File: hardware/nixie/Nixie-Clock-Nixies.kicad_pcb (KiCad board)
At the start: 2 copper layers, 21 parts, among them J1 Nixies-Connector

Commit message: Add screw terminals for I/O, Improve PCB layout
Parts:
- moved J1 91.8 mm to (237.5, 64.8)
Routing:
- net /a2: track 94.3 -> 181.4 mm
- net /a1: track 97.5 -> 182.3 mm
- net /a3: track 19.4 -> 100.6 mm
- net /a4: track 18.3 -> 99.1 mm
- net /a5: track 74.9 -> 28.6 mm
- net /a6: track 74.4 -> 30.9 mm
- net /c6: track 270.5 -> 232.1 mm
- net /c1: track 228.9 -> 209.0 mm
- net /da: track 107.4 -> 126.0 mm
- net Net-(N6-PadA3): track 29.2 -> 44.3 mm
- net /c3: track 240.3 -> 227.5 mm
- net /c4: track 237.2 -> 225.9 mm
- net /c2: track 242.3 -> 232.6 mm
- net Net-(N4-PadA3): track 48.5 -> 39.4 mm
- net /c5: track 224.6 -> 218.3 mm
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
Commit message: Add Mounting Holes to PCB, Improve Routing, Add power pin header, Use correct connector footprint
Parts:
- added H1: MountingHole, MountingHole:MountingHole_2.7mm_M2.5, F.Cu at (25.4, 24.1)
- added H2: MountingHole, MountingHole:MountingHole_2.7mm_M2.5, F.Cu at (243.8, 24.1)
- added H3: MountingHole, MountingHole:MountingHole_2.7mm_M2.5, F.Cu at (25.4, 58.4)
- added H4: MountingHole, MountingHole:MountingHole_2.7mm_M2.5, F.Cu at (243.8, 58.4)
- J1: footprint Connector_PinHeader_2.54mm:PinHeader_2x10_P2.54mm_Horizontal -> nixie-clock:PinHeader_2x10_P2.54mm_Horizontal_with_Interlock
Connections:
- J1 pad 18: Net-(J1-Pad18) -> (no net)
- J1 pad 7: Net-(J1-Pad7) -> (no net)

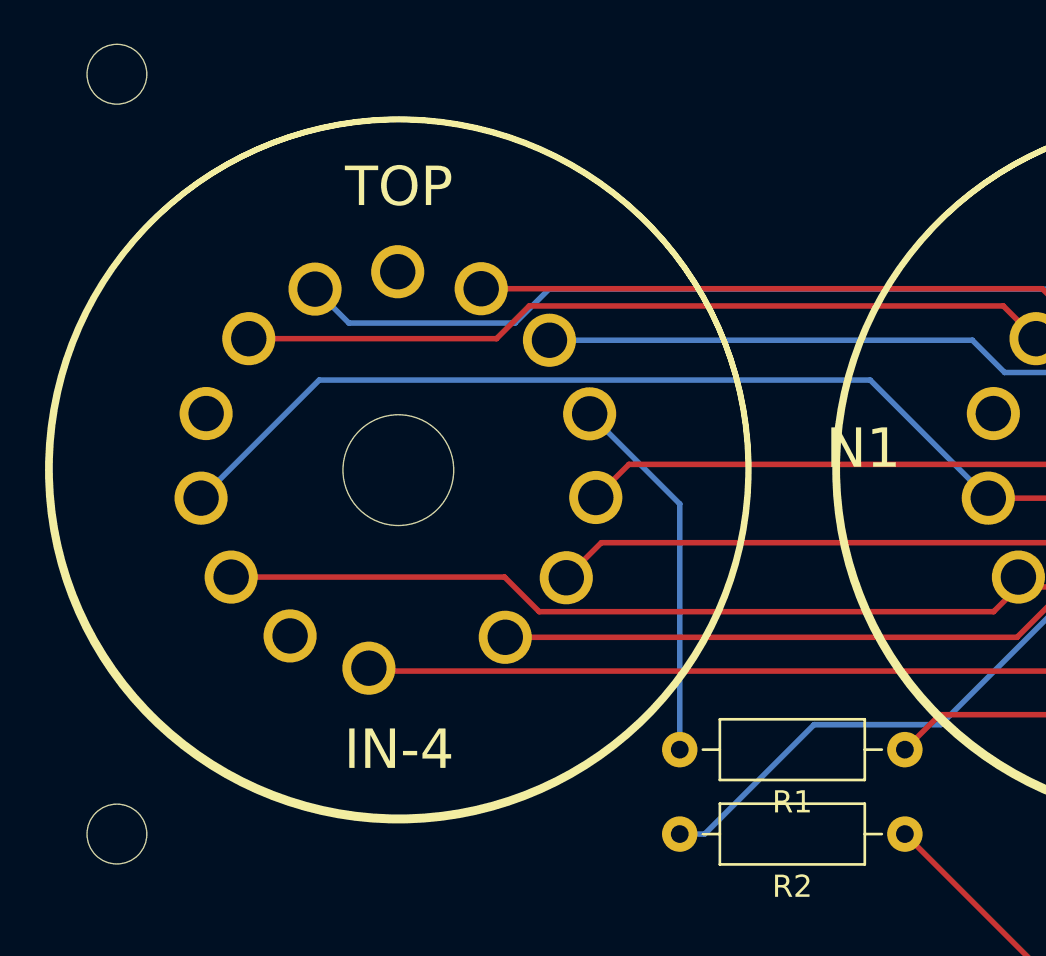
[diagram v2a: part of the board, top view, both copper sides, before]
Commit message: Fix libraries used in Nixie-Clock-Nixies
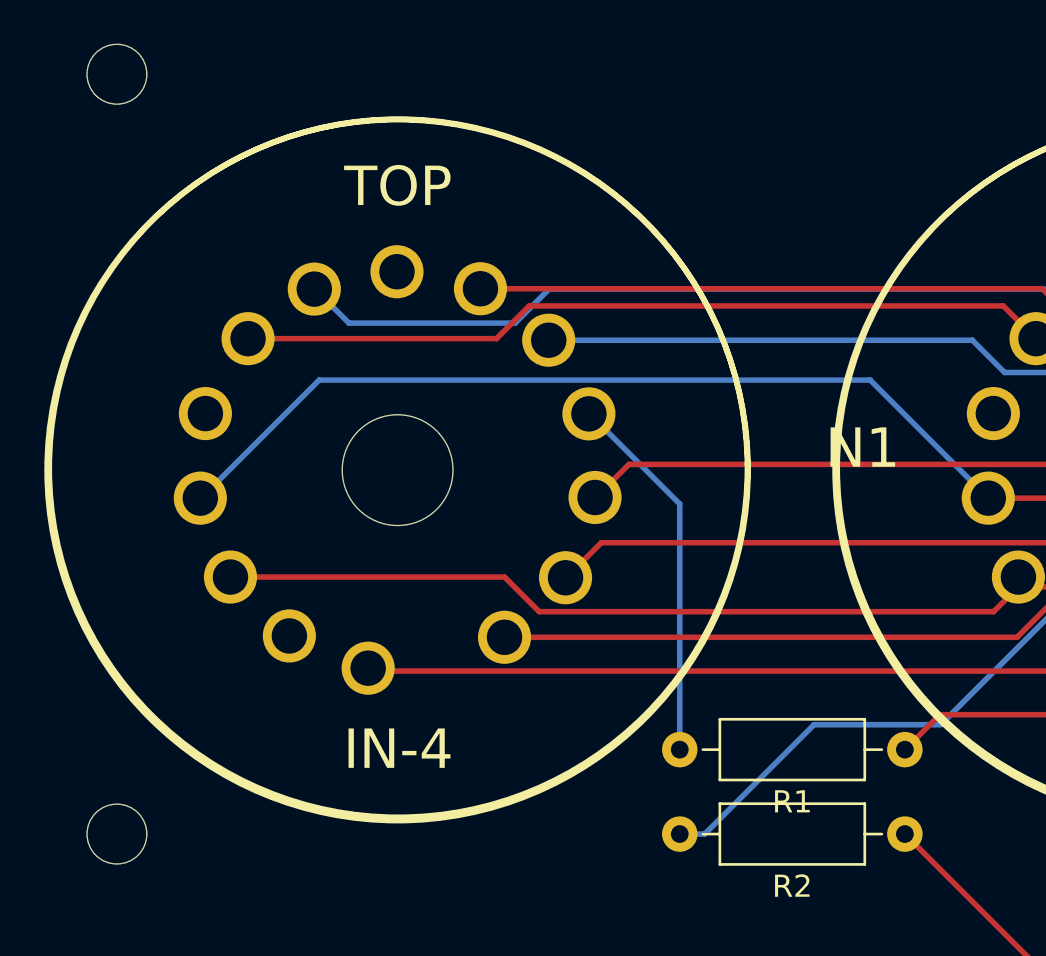
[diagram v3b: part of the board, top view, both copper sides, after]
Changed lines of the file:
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@@
   )
   (page A4)
+  (title_block
+    (title "Nixie-Clock: Nixies")
+    (date 2021-12-25)
+    (rev 1.0)
+    (company "Konrad Mösch")
+  )
   (layers
     (0 F.Cu signal)
@@
     (add_net /da)
     (add_net /dc)
-    (add_net "Net-(J1-Pad18)")
-    (add_net "Net-(J1-Pad7)")
     (add_net "Net-(N1-PadA3)")
     (add_net "Net-(N10-PadA)")
@@
     (add_net "Net-(N9-PadA)")
   )
+  (module nixies-us:nixies-us-IN-4-DSUB (layer F.Cu)
+    (at 38.1 41.91)
+    (descr "MAY BE USED WITH SOCKET: PL31-P")
+    (tags "MAY BE USED WITH SOCKET: PL31-P")
+    (attr virtual)
+    (fp_text reference N1 (at 20.955 -0.889) (layer F.SilkS)
+      (effects (font (size 1.778 1.778) (thickness 0.1524)))
+    )
+    (fp_text value IN-4 (at 0 12.7) (layer F.SilkS)
+      (effects (font (size 1.778 1.778) (thickness 0.1524)))
+    )
+    (fp_circle (center 0 0) (end 0 -2.54) (layer F.Mask) (width 0.0254))
+    (fp_circle (center 0 0) (end 0 -1.27) (layer F.Mask) (width 2.54))
+    (fp_circle (center 0 0) (end 0 -1.27) (layer B.Mask) (width 2.54))
+    (fp_circle (center -0.03302 0.08636) (end -0.03302 -2.45364) (layer Dwgs.User) (width 0.0254))
+    (fp_circle (center -0.03302 0.08636) (end -0.03302 -15.73022) (layer F.SilkS) (width 0.254))
+    (fp_circle (center 0 0) (end 0 -15.75308) (layer F.SilkS) (width 0.254))
+    (fp_text user TOP (at 0 -12.7) (layer F.SilkS)
+      (effects (font (size 1.778 1.778) (thickness 0.1524)))
+    )
+    (pad "" np_thru_hole circle (at -0.03302 0.08636) (size 4.99872 4.99872) (drill 4.99872) (layers *.Cu *.Mask))
+    (pad N/C thru_hole circle (at -0.06096 -8.86714) (size 2.39776 2.39776) (drill 1.59766) (layers *.Cu *.Mask))
+    (pad A3 thru_hole circle (at 8.60044 -2.45364) (size 2.39776 2.39776) (drill 1.59766) (layers *.Cu *.Mask)
+      (net 19 "Net-(N1-PadA3)"))
+    (pad A2 thru_hole circle (at -8.70712 -2.46634) (size 2.39776 2.39776) (drill 1.59766) (layers *.Cu *.Mask))
+    (pad A1 thru_hole circle (at -4.91744 7.5692) (size 2.39776 2.39776) (drill 1.59766) (layers *.Cu *.Mask))
+    (pad 9 thru_hole circle (at 6.78688 -5.77596) (size 2.39776 2.39776) (drill 1.59766) (layers *.Cu *.Mask)
+      (net 7 /c9))
+    (pad 8 thru_hole circle (at 8.8773 1.3208) (size 2.39776 2.39776) (drill 1.59766) (layers *.Cu *.Mask)
+      (net 8 /c8))
+    (pad 7 thru_hole circle (at 3.70586 -8.10006) (size 2.39776 2.39776) (drill 1.59766) (layers *.Cu *.Mask)
+      (net 9 /c7))
+    (pad 6 thru_hole circle (at 7.54634 4.94284) (size 2.39776 2.39776) (drill 1.59766) (layers *.Cu *.Mask)
+      (net 10 /c6))
+    (pad 5 thru_hole circle (at -7.57682 4.91236) (size 2.39776 2.39776) (drill 1.59766) (layers *.Cu *.Mask)
+      (net 11 /c5))
+    (pad 4 thru_hole circle (at 4.79298 7.63016) (size 2.39776 2.39776) (drill 1.59766) (layers *.Cu *.Mask)
+      (net 12 /c4))
+    (pad 3 thru_hole circle (at -8.93572 1.35128) (size 2.39776 2.39776) (drill 1.59766) (layers *.Cu *.Mask)
+      (net 13 /c3))
+    (pad 2 thru_hole circle (at -6.7818 -5.84708) (size 2.39776 2.39776) (drill 1.59766) (layers *.Cu *.Mask)
+      (net 14 /c2))
+    (pad 1 thru_hole circle (at -1.36144 9.02462) (size 2.39776 2.39776) (drill 1.59766) (layers *.Cu *.Mask)
+      (net 15 /c1))
+    (pad 0 thru_hole circle (at -3.79222 -8.08228) (size 2.39776 2.39776) (drill 1.59766) (layers *.Cu *.Mask)
+      (net 16 /c0))
+  )
   (module nixie-clock:PinHeader_2x10_P2.54mm_Horizontal_with_Interlock (layer F.Cu)
     (at 237.49 64.77 270)
@@
     )
     (fp_text value Nixies-Connector (at 5.655 25.13 90) (layer F.Fab)
-      (effects (font (size 1 1) (thickness 0.15)))
-    )
-    (fp_text user %R (at 5.31 11.43) (layer F.Fab)
       (effects (font (size 1 1) (thickness 0.15)))
     )
@@
     (fp_line (start -2.54 34.29) (end 15.24 34.29) (layer F.SilkS) (width 0.12))
     (fp_line (start 15.24 -11.43) (end 15.24 34.29) (layer F.SilkS) (width 0.12))
+    (fp_text user %R (at 5.31 11.43) (layer F.Fab)
+      (effects (font (size 1 1) (thickness 0.15)))
+    )
     (pad 20 thru_hole oval (at 2.54 22.86 270) (size 1.7 1.7) (drill 1) (layers *.Cu *.Mask)
       (net 17 /dc))
@@
       (effects (font (size 1 1) (thickness 0.15)))
     )
-    (fp_text user %R (at 0.3 0) (layer F.Fab)
-      (effects (font (size 1 1) (thickness 0.15)))
-    )
     (fp_circle (center 0 0) (end 2.7 0) (layer Cmts.User) (width 0.15))
     (fp_circle (center 0 0) (end 2.95 0) (layer F.CrtYd) (width 0.05))
+    (fp_text user %R (at 0.3 0) (layer F.Fab)
+      (effects (font (size 1 1) (thickness 0.15)))
+    )
     (pad 1 np_thru_hole circle (at 0 0) (size 2.7 2.7) (drill 2.7) (layers *.Cu *.Mask))
   )
@@
       (effects (font (size 1 1) (thickness 0.15)))
     )
-    (fp_text user %R (at 0.3 0) (layer F.Fab)
-      (effects (font (size 1 1) (thickness 0.15)))
-    )
     (fp_circle (center 0 0) (end 2.7 0) (layer Cmts.User) (width 0.15))
     (fp_circle (center 0 0) (end 2.95 0) (layer F.CrtYd) (width 0.05))
+    (fp_text user %R (at 0.3 0) (layer F.Fab)
+      (effects (font (size 1 1) (thickness 0.15)))
+    )
     (pad 1 np_thru_hole circle (at 0 0) (size 2.7 2.7) (drill 2.7) (layers *.Cu *.Mask))
   )
@@
       (effects (font (size 1 1) (thickness 0.15)))
     )
-    (fp_text user %R (at 0.3 0) (layer F.Fab)
-      (effects (font (size 1 1) (thickness 0.15)))
-    )
     (fp_circle (center 0 0) (end 2.7 0) (layer Cmts.User) (width 0.15))
     (fp_circle (center 0 0) (end 2.95 0) (layer F.CrtYd) (width 0.05))
+    (fp_text user %R (at 0.3 0) (layer F.Fab)
+      (effects (font (size 1 1) (thickness 0.15)))
+    )
     (pad 1 np_thru_hole circle (at 0 0) (size 2.7 2.7) (drill 2.7) (layers *.Cu *.Mask))
   )
@@
       (effects (font (size 1 1) (thickness 0.15)))
     )
-    (fp_text user %R (at 0.3 0) (layer F.Fab)
-      (effects (font (size 1 1) (thickness 0.15)))
-    )
     (fp_circle (center 0 0) (end 2.7 0) (layer Cmts.User) (width 0.15))
     (fp_circle (center 0 0) (end 2.95 0) (layer F.CrtYd) (width 0.05))
+    (fp_text user %R (at 0.3 0) (layer F.Fab)
+      (effects (font (size 1 1) (thickness 0.15)))
+    )
     (pad 1 np_thru_hole circle (at 0 0) (size 2.7 2.7) (drill 2.7) (layers *.Cu *.Mask))
   )
@@
   )
   (module nixies-us:nixies-us-IN-4-DSUB (layer F.Cu)
-    (at 38.133 41.91)
-    (descr "MAY BE USED WITH SOCKET: PL31-P")
-    (tags "MAY BE USED WITH SOCKET: PL31-P")
-    (attr virtual)
-    (fp_text reference N1 (at 20.955 -0.889) (layer F.SilkS)
-      (effects (font (size 1.778 1.778) (thickness 0.1524)))
-    )
-    (fp_text value IN-4 (at 0 12.7) (layer F.SilkS)
-      (effects (font (size 1.778 1.778) (thickness 0.1524)))
-    )
-    (fp_circle (center 0 0) (end 0 -15.75308) (layer F.SilkS) (width 0.254))
-    (fp_circle (center -0.03302 0.08636) (end -0.03302 -15.73022) (layer F.SilkS) (width 0.254))
-    (fp_circle (center -0.03302 0.08636) (end -0.03302 -2.45364) (layer Dwgs.User) (width 0.0254))
-    (fp_circle (center 0 0) (end 0 -1.27) (layer B.Mask) (width 2.54))
-    (fp_circle (center 0 0) (end 0 -1.27) (layer F.Mask) (width 2.54))
-    (fp_circle (center 0 0) (end 0 -2.54) (layer F.Mask) (width 0.0254))
-    (fp_text user TOP (at 0 -12.7) (layer F.SilkS)
-      (effects (font (size 1.778 1.778) (thickness 0.1524)))
-    )
-    (pad 0 thru_hole circle (at -3.79222 -8.08228) (size 2.39776 2.39776) (drill 1.59766) (layers *.Cu *.Mask)
-      (net 16 /c0))
-    (pad 1 thru_hole circle (at -1.36144 9.02462) (size 2.39776 2.39776) (drill 1.59766) (layers *.Cu *.Mask)
-      (net 15 /c1))
-    (pad 2 thru_hole circle (at -6.7818 -5.84708) (size 2.39776 2.39776) (drill 1.59766) (layers *.Cu *.Mask)
-      (net 14 /c2))
-    (pad 3 thru_hole circle (at -8.93572 1.35128) (size 2.39776 2.39776) (drill 1.59766) (layers *.Cu *.Mask)
-      (net 13 /c3))
-    (pad 4 thru_hole circle (at 4.79298 7.63016) (size 2.39776 2.39776) (drill 1.59766) (layers *.Cu *.Mask)
-      (net 12 /c4))
-    (pad 5 thru_hole circle (at -7.57682 4.91236) (size 2.39776 2.39776) (drill 1.59766) (layers *.Cu *.Mask)
-      (net 11 /c5))
-    (pad 6 thru_hole circle (at 7.54634 4.94284) (size 2.39776 2.39776) (drill 1.59766) (layers *.Cu *.Mask)
-      (net 10 /c6))
-    (pad 7 thru_hole circle (at 3.70586 -8.10006) (size 2.39776 2.39776) (drill 1.59766) (layers *.Cu *.Mask)
-      (net 9 /c7))
-    (pad 8 thru_hole circle (at 8.8773 1.3208) (size 2.39776 2.39776) (drill 1.59766) (layers *.Cu *.Mask)
-      (net 8 /c8))
-    (pad 9 thru_hole circle (at 6.78688 -5.77596) (size 2.39776 2.39776) (drill 1.59766) (layers *.Cu *.Mask)
-      (net 7 /c9))
-    (pad A1 thru_hole circle (at -4.91744 7.5692) (size 2.39776 2.39776) (drill 1.59766) (layers *.Cu *.Mask))
-    (pad A2 thru_hole circle (at -8.70712 -2.46634) (size 2.39776 2.39776) (drill 1.59766) (layers *.Cu *.Mask))
-    (pad A3 thru_hole circle (at 8.60044 -2.45364) (size 2.39776 2.39776) (drill 1.59766) (layers *.Cu *.Mask)
-      (net 19 "Net-(N1-PadA3)"))
-    (pad N/C thru_hole circle (at -0.06096 -8.86714) (size 2.39776 2.39776) (drill 1.59766) (layers *.Cu *.Mask))
-    (pad "" np_thru_hole circle (at -0.03302 0.08636) (size 4.99872 4.99872) (drill 4.99872) (layers *.Cu *.Mask))
-  )
-  (module nixies-us:nixies-us-IN-4-DSUB (layer F.Cu)
